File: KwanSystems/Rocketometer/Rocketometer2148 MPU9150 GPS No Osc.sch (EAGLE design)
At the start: 65 parts, among them J001 USB_MICROB_JSTGCT, J301 JST 2mm, J401 M07, J501 GP-2106, J701 MICROSD-SOCKET, Q050 PMOS, Q501 SSM6N58NU, Q502 SSM6N58NU, U101 BMP180, U201 5319 3.3V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

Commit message: j
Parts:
- removed C403, C405: 22pF, SparkFun:CAP0402-CAP
- removed Q501, Q502: SSM6N58NU, KwanSystems:SSM6N58NU
- removed R302: 1M, KwanSystems:RP2EXB24V
- removed R501, R502: 10k, KwanSystems:RP404
- removed Y402: 32kiHz, KwanSystems:ABS06
- added S441: B3U-1100P, KwanSystems:B3U-1100P
- added U502: TXB0104RUT, KwanSystems:TXB0104RUT
- J401: device SparkFun-Connectors:M081X08 -> SparkFun-Connectors:M11PTH
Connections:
- net N$4 renamed CHARGE_STAT-
- net N$8 renamed VEXT
- removed net N$3: D301.A, R053D.1
- removed net RTXC1: C403.2, U401.RTXC1, Y402.2
- removed net RTXC2: C405.1, U401.RTXC2, Y402.1
- new net CHARGE_STAT+: D301.A, R053B.1
- new net EXT: J401.11, U401.(AD1.7/CAP0.0/MAT0.0)P0.22
- net 1.8V: now also U502HEAD.OE, U502HEAD.VCC_LO; no longer Q501A.G, Q501B.G, Q502A.G, Q502B.G, R501B.2, R501C.2, R502B.2, R502C.2
- net 1PPS_I: now also U502D.IO_LO; no longer Q502B.S, R502B.1
- net BATLVL: no longer R302A.2, R302B.2
- net BSL: now also J401.8, S441S.1; no longer J401.5
- net CONN_D+: now also R053A.2; no longer R053B.2
- net EN: no longer U501.EN
- net GND: now also R053C.2, S441G.1, S441S.2, U502HEAD.GND; no longer C403.1, C405.2, R053A.1, R302A.1
- net N$6: now also R053A.1; no longer R053B.1
- net N$7: now also R053C.1; no longer R053A.2
- net ONOFF: now also U502C.IO_HI; no longer Q502A.D, R502A.1
- net ONOFF_I: now also U502C.IO_LO; no longer Q502A.S, R502C.1
- net PPS: now also U502D.IO_HI; no longer Q502B.D, R502D.1
- net RX_GPS: now also J401.5, U502B.IO_HI; no longer J401.6, Q501A.D, R501D.1
- net RX_I: now also U502B.IO_LO; no longer Q501A.S, R501B.1
- net SCL0: now also J401.9
- net SDA0: now also J401.10
- net TX_GPS: now also J401.6, U502A.IO_HI; no longer J401.7, Q501B.D, R501A.1
- net TX_O: now also U502A.IO_LO; no longer Q501B.S, R501C.1
- net USBD+: now also C023A.1; no longer C023B.1
- net USBD-: now also C023B.1; no longer C023A.1
- net VBUS: now also R053B.2; no longer R053D.2
- net VCC: now also J401.7, U401.RTXC1, U501.EN, U502HEAD.VCC_HI; no longer J401.8, R501A.2, R501D.2, R502A.2, R502D.2
- net VLIPO: no longer R302B.1
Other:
- note removed: "OR Y401/C461/C462"
- note removed: "Place either Y403/C404"
- note removed: "but not both groups"
- moved on the sheet: C023A, C023B, C449, C504, C505, R053A, R053B, R053D

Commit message: Finally found a complete solution
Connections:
- removed net N$6: D050.A, Q050.D, R053A.1
- removed net N$7: D050.C, R053C.1
- new net USBLIGHT+: D050.A, R053B.2
- new net USBON+: Q050.D, R053A.2, R053B.1
- net CHARGE_STAT+: now also R053C.2; no longer R053B.1
- net CONN_D+: now also R023A.2, R053A.1; no longer R023B.1, R053A.2
- net CONN_D-: now also R023B.2; no longer R023A.1
- net GND: now also D050.C; no longer R053C.2
- net USBD+: now also R023A.1; no longer R023B.2
- net USBD-: now also R023B.1; no longer R023A.2
- net USB_SOFTCONNECT: now also R015A.1; no longer R015A.2
- net VBUS: now also R053C.1; no longer R053B.2
- net VCC: now also R015A.2; no longer R015A.1
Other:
- moved on the sheet: R023A, R023B, R053A, R053B, R053C
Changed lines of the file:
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@@
 <attribute name="DIGIKEY" x="40.64" y="22.86" size="1.778" layer="96" display="off"/>
 </instance>
-<instance part="D050" gate="G$1" x="22.86" y="66.04" smashed="yes" rot="MR0">
-<attribute name="NAME" x="19.304" y="61.468" size="1.778" layer="95" rot="MR90"/>
-<attribute name="VALUE" x="27.305" y="61.468" size="1.778" layer="96" rot="MR90"/>
-<attribute name="DIGIKEY" x="22.86" y="66.04" size="1.778" layer="96" display="off"/>
+<instance part="D050" gate="G$1" x="22.86" y="48.26" smashed="yes" rot="MR0">
+<attribute name="VALUE" x="27.305" y="43.688" size="1.778" layer="96" rot="MR90"/>
+<attribute name="DIGIKEY" x="22.86" y="48.26" size="1.778" layer="96" display="off"/>
 </instance>
 <instance part="Q050" gate="G$1" x="22.86" y="76.2" rot="R180">
@@
 <attribute name="DIGIKEY" x="205.74" y="40.64" size="1.778" layer="96" display="off"/>
 </instance>
-<instance part="R023" gate="A" x="55.88" y="38.1"/>
-<instance part="R023" gate="B" x="48.26" y="35.56"/>
-<instance part="R053" gate="A" x="17.78" y="55.88" rot="R270">
-<attribute name="DIGIKEY" x="17.78" y="55.88" size="1.778" layer="96" display="off"/>
-</instance>
-<instance part="R053" gate="C" x="22.86" y="48.26" rot="R270"/>
+<instance part="R023" gate="B" x="55.88" y="38.1"/>
+<instance part="R023" gate="A" x="48.26" y="35.56"/>
+<instance part="R053" gate="A" x="17.78" y="58.42" rot="R270">
+<attribute name="DIGIKEY" x="17.78" y="58.42" size="1.778" layer="96" display="off"/>
+</instance>
+<instance part="R053" gate="B" x="22.86" y="58.42" rot="R90"/>
 <instance part="C023" gate="A" x="71.12" y="20.32">
 <attribute name="DIGIKEY" x="71.12" y="20.32" size="1.778" layer="96" display="off"/>
@@
 </instance>
 <instance part="R015" gate="B" x="63.5" y="40.64" rot="R180"/>
-<instance part="R053" gate="B" x="114.3" y="27.94" rot="R90"/>
+<instance part="R053" gate="C" x="114.3" y="27.94" rot="R90"/>
 <instance part="D401" gate="B" x="218.44" y="-58.42" rot="R270">
 <attribute name="DIGIKEY" x="218.44" y="-58.42" size="1.778" layer="96" display="off"/>
@@
 <wire x1="276.86" y1="86.36" x2="276.86" y2="88.9" width="0.1524" layer="91"/>
 <wire x1="276.86" y1="45.72" x2="276.86" y2="86.36" width="0.1524" layer="91"/>
-<wire x1="22.86" y1="86.36" x2="38.1" y2="86.36" width="0.1524" layer="91"/>
-<wire x1="38.1" y1="86.36" x2="276.86" y2="86.36" width="0.1524" layer="91"/>
+<wire x1="22.86" y1="86.36" x2="38.1" y2="76.2" width="0.1524" layer="91"/>
+<wire x1="38.1" y1="76.2" x2="276.86" y2="86.36" width="0.1524" layer="91"/>
 <wire x1="22.86" y1="86.36" x2="22.86" y2="81.28" width="0.1524" layer="91"/>
 <wire x1="261.62" y1="45.72" x2="276.86" y2="45.72" width="0.1524" layer="91"/>
@@
 <pinref part="U201" gate="G$1" pin="VOUT"/>
 <pinref part="C205" gate="G$1" pin="1"/>
-<pinref part="R015" gate="A" pin="1"/>
-<junction x="38.1" y="86.36"/>
+<pinref part="R015" gate="A" pin="2"/>
+<junction x="38.1" y="76.2"/>
 </segment>
 <segment>
@@
 <wire x1="12.7" y1="12.7" x2="12.7" y2="15.24" width="0.1524" layer="91"/>
 <wire x1="40.64" y1="15.24" x2="40.64" y2="17.78" width="0.1524" layer="91"/>
-<wire x1="22.86" y1="43.18" x2="22.86" y2="15.24" width="0.1524" layer="91"/>
-<wire x1="22.86" y1="15.24" x2="12.7" y2="15.24" width="0.1524" layer="91"/>
 <wire x1="71.12" y1="17.78" x2="71.12" y2="15.24" width="0.1524" layer="91"/>
 <wire x1="71.12" y1="15.24" x2="40.64" y2="15.24" width="0.1524" layer="91"/>
 <wire x1="40.64" y1="15.24" x2="22.86" y2="15.24" width="0.1524" layer="91"/>
+<wire x1="22.86" y1="15.24" x2="12.7" y2="15.24" width="0.1524" layer="91"/>
 <wire x1="81.28" y1="17.78" x2="81.28" y2="15.24" width="0.1524" layer="91"/>
 <wire x1="81.28" y1="15.24" x2="71.12" y2="15.24" width="0.1524" layer="91"/>
@@
 <junction x="12.7" y="15.24"/>
 <junction x="40.64" y="15.24"/>
-<junction x="22.86" y="15.24"/>
 <junction x="71.12" y="15.24"/>
 <junction x="81.28" y="15.24"/>
@@
 <pinref part="U301" gate="G$1" pin="VSS"/>
 <pinref part="S201" gate="B" pin="P$1"/>
-<pinref part="R053" gate="C" pin="2"/>
 <pinref part="C023" gate="A" pin="2"/>
 <pinref part="C023" gate="B" pin="2"/>
+<pinref part="D050" gate="G$1" pin="C"/>
+<wire x1="22.86" y1="43.18" x2="22.86" y2="15.24" width="0.1524" layer="91"/>
+<junction x="22.86" y="15.24"/>
 </segment>
 <segment>
@@
 <wire x1="33.02" y1="33.02" x2="101.6" y2="33.02" width="0.1524" layer="91"/>
 <wire x1="101.6" y1="30.48" x2="101.6" y2="33.02" width="0.1524" layer="91"/>
-<wire x1="124.46" y1="33.02" x2="114.3" y2="33.02" width="0.1524" layer="91"/>
-<wire x1="114.3" y1="33.02" x2="109.22" y2="33.02" width="0.1524" layer="91"/>
+<wire x1="124.46" y1="33.02" x2="114.3" y2="22.86" width="0.1524" layer="91"/>
+<wire x1="114.3" y1="22.86" x2="109.22" y2="33.02" width="0.1524" layer="91"/>
 <junction x="40.64" y="40.64"/>
 <junction x="33.02" y="40.64"/>
 <junction x="101.6" y="33.02"/>
 <junction x="109.22" y="33.02"/>
-<junction x="114.3" y="33.02"/>
+<junction x="114.3" y="22.86"/>
 <label x="91.44" y="33.02" size="1.778" layer="95"/>
 <pinref part="D302" gate="G$1" pin="A1"/>
@@
 <pinref part="U301" gate="G$1" pin="VIN"/>
 <pinref part="R015" gate="B" pin="2"/>
-<pinref part="R053" gate="B" pin="2"/>
+<pinref part="R053" gate="C" pin="1"/>
 </segment>
 </net>
@@
 </segment>
 <segment>
-<wire x1="60.96" y1="38.1" x2="81.28" y2="38.1" width="0.1524" layer="91"/>
+<wire x1="50.8" y1="38.1" x2="81.28" y2="38.1" width="0.1524" layer="91"/>
 <wire x1="81.28" y1="38.1" x2="81.28" y2="63.5" width="0.1524" layer="91"/>
 <wire x1="81.28" y1="38.1" x2="81.28" y2="25.4" width="0.1524" layer="91"/>
 <junction x="81.28" y="38.1"/>
 <label x="81.28" y="63.5" size="1.778" layer="95" rot="MR270"/>
-<pinref part="R023" gate="A" pin="2"/>
+<pinref part="R023" gate="B" pin="1"/>
 <pinref part="C023" gate="B" pin="1"/>
 </segment>
@@
 </segment>
 <segment>
-<wire x1="53.34" y1="35.56" x2="71.12" y2="35.56" width="0.1524" layer="91"/>
+<wire x1="43.18" y1="35.56" x2="71.12" y2="35.56" width="0.1524" layer="91"/>
 <wire x1="71.12" y1="35.56" x2="71.12" y2="43.18" width="0.1524" layer="91"/>
 <wire x1="71.12" y1="43.18" x2="78.74" y2="43.18" width="0.1524" layer="91"/>
@@
 <junction x="71.12" y="35.56"/>
 <label x="78.74" y="63.5" size="1.778" layer="95" rot="MR270"/>
-<pinref part="R023" gate="B" pin="2"/>
+<pinref part="R023" gate="A" pin="1"/>
 <pinref part="C023" gate="A" pin="1"/>
 </segment>
@@
 </segment>
 <segment>
-<wire x1="30.48" y1="76.2" x2="38.1" y2="76.2" width="0.1524" layer="91"/>
-<wire x1="38.1" y1="76.2" x2="38.1" y2="45.72" width="0.1524" layer="91"/>
+<wire x1="30.48" y1="76.2" x2="38.1" y2="86.36" width="0.1524" layer="91"/>
+<wire x1="38.1" y1="86.36" x2="38.1" y2="45.72" width="0.1524" layer="91"/>
 <wire x1="38.1" y1="45.72" x2="76.2" y2="45.72" width="0.1524" layer="91"/>
 <wire x1="76.2" y1="45.72" x2="76.2" y2="63.5" width="0.1524" layer="91"/>
 <label x="76.2" y="63.5" size="1.778" layer="95" rot="MR270"/>
 <pinref part="Q050" gate="G$1" pin="G"/>
-<pinref part="R015" gate="A" pin="2"/>
-<junction x="38.1" y="76.2"/>
+<pinref part="R015" gate="A" pin="1"/>
+<junction x="38.1" y="86.36"/>
 </segment>
 </net>
@@
 <net name="CONN_D-" class="0">
 <segment>
-<wire x1="2.54" y1="38.1" x2="50.8" y2="38.1" width="0.1524" layer="91"/>
+<wire x1="2.54" y1="38.1" x2="60.96" y2="38.1" width="0.1524" layer="91"/>
 <pinref part="J001" gate="G$1" pin="D-"/>
-<pinref part="R023" gate="A" pin="1"/>
+<pinref part="R023" gate="B" pin="2"/>
 </segment>
 </net>
@@
 <segment>
 <wire x1="2.54" y1="35.56" x2="17.78" y2="35.56" width="0.1524" layer="91"/>
-<wire x1="17.78" y1="35.56" x2="43.18" y2="35.56" width="0.1524" layer="91"/>
-<wire x1="17.78" y1="50.8" x2="17.78" y2="35.56" width="0.1524" layer="91"/>
+<wire x1="17.78" y1="35.56" x2="53.34" y2="35.56" width="0.1524" layer="91"/>
+<wire x1="17.78" y1="63.5" x2="17.78" y2="35.56" width="0.1524" layer="91"/>
 <junction x="17.78" y="35.56"/>
 <pinref part="J001" gate="G$1" pin="D+"/>
-<pinref part="R023" gate="B" pin="1"/>
-<pinref part="R053" gate="A" pin="2"/>
-</segment>
-</net>
-<net name="N$7" class="0">
-<segment>
-<wire x1="22.86" y1="60.96" x2="22.86" y2="53.34" width="0.1524" layer="91"/>
-<pinref part="D050" gate="G$1" pin="C"/>
-<pinref part="R053" gate="C" pin="1"/>
+<pinref part="R023" gate="A" pin="2"/>
+<pinref part="R053" gate="A" pin="1"/>
 </segment>
 </net>
 <net name="CHARGE_STAT+" class="0">
 <segment>
-<wire x1="114.3" y1="22.86" x2="114.3" y2="20.32" width="0.1524" layer="91"/>
+<wire x1="114.3" y1="33.02" x2="114.3" y2="20.32" width="0.1524" layer="91"/>
 <wire x1="114.3" y1="20.32" x2="121.92" y2="20.32" width="0.1524" layer="91"/>
 <pinref part="D301" gate="G$1" pin="A"/>
-<pinref part="R053" gate="B" pin="1"/>
+<pinref part="R053" gate="C" pin="2"/>
 </segment>
 </net>
@@
 </segment>
 </net>
-<net name="N$6" class="0">
+<net name="USBON+" class="0">
 <segment>
 <wire x1="22.86" y1="71.12" x2="22.86" y2="68.58" width="0.1524" layer="91"/>
-<wire x1="22.86" y1="68.58" x2="17.78" y2="68.58" width="0.1524" layer="91"/>
-<wire x1="17.78" y1="68.58" x2="17.78" y2="60.96" width="0.1524" layer="91"/>
-<junction x="22.86" y="68.58"/>
 <pinref part="Q050" gate="G$1" pin="D"/>
-<pinref part="D050" gate="G$1" pin="A"/>
-<pinref part="R053" gate="A" pin="1"/>
+<pinref part="R053" gate="A" pin="2"/>
+<wire x1="17.78" y1="53.34" x2="17.78" y2="68.58" width="0.1524" layer="91"/>
+<wire x1="17.78" y1="68.58" x2="22.86" y2="68.58" width="0.1524" layer="91"/>
+<pinref part="R053" gate="B" pin="1"/>
+<wire x1="22.86" y1="68.58" x2="22.86" y2="53.34" width="0.1524" layer="91"/>
 </segment>
 </net>
@@
 </segment>
 </net>
+<net name="USBLIGHT+" class="0">
+<segment>
+<pinref part="D050" gate="G$1" pin="A"/>
+<pinref part="R053" gate="B" pin="2"/>
+<wire x1="22.86" y1="63.5" x2="22.86" y2="50.8" width="0.1524" layer="91"/>
+</segment>
+</net>

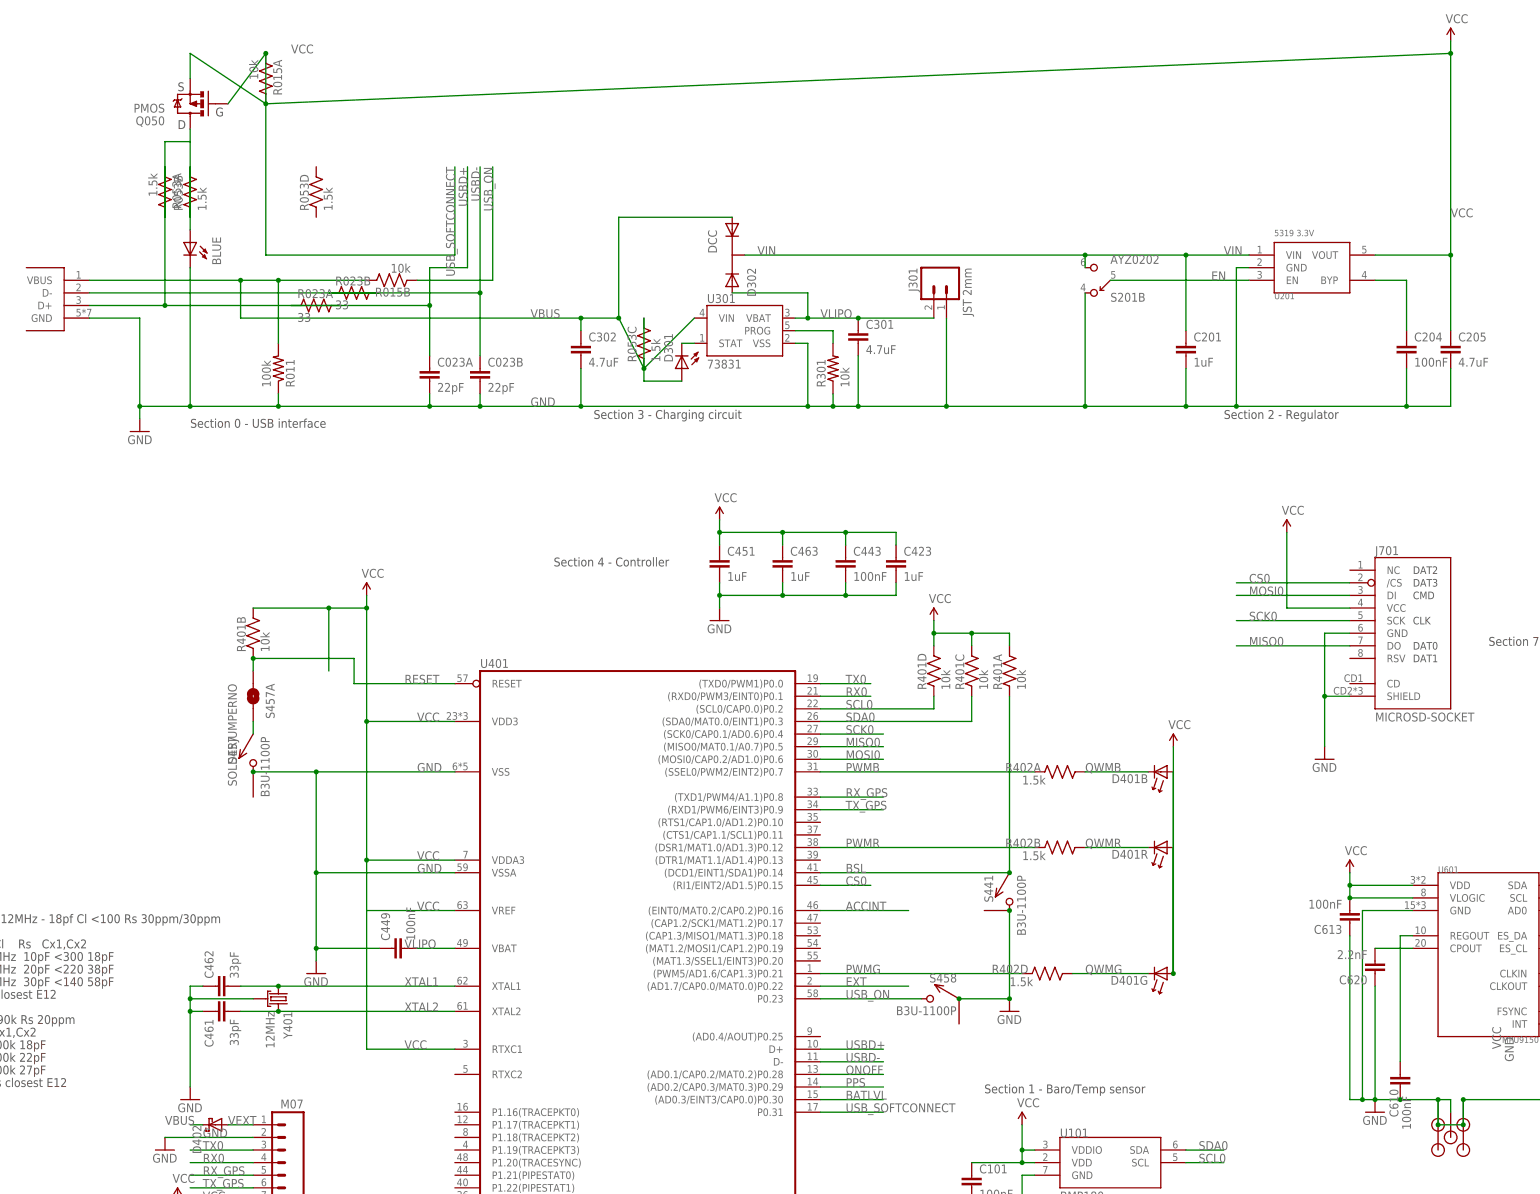
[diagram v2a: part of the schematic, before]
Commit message: Added new feature to NavCalc
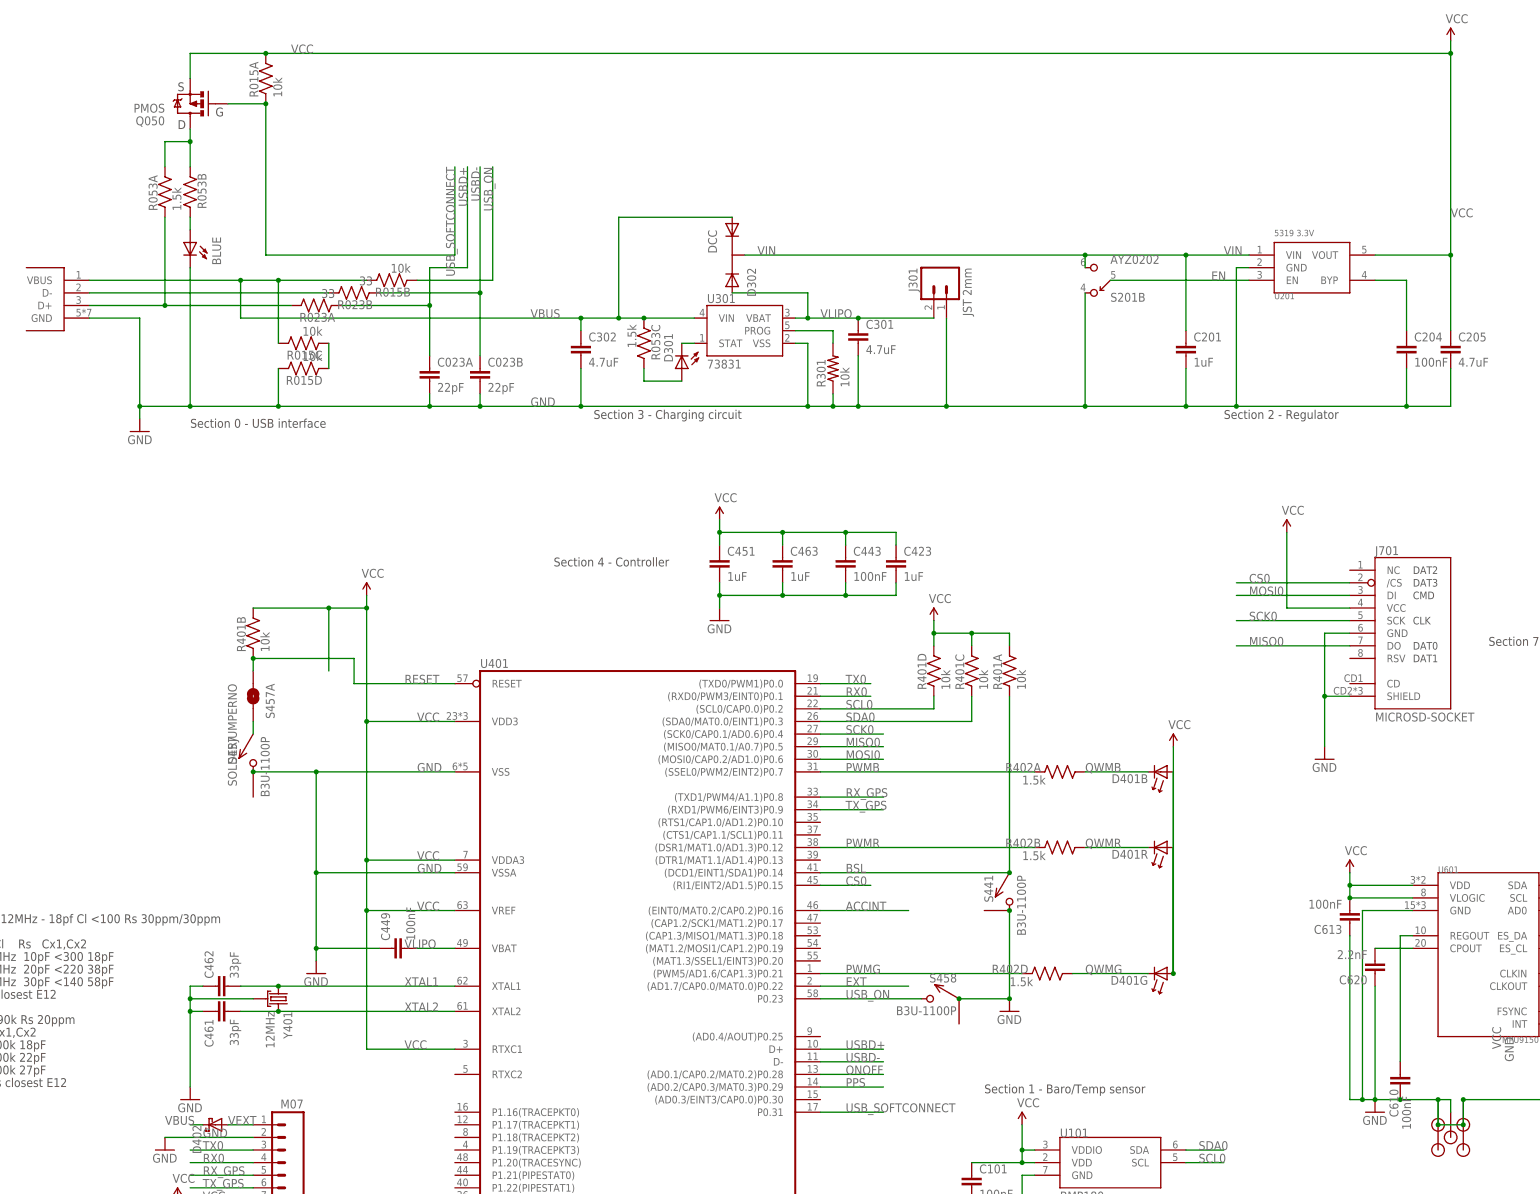
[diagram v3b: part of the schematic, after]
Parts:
- removed R011: 100k, SparkFun:RESISTOR0402-RES
- R015: device KwanSystems:RP2EXB24V -> KwanSystems:RP404
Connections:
- removed net BATLVL: U401.(AD0.3/EINT3/CAP0.0)P0.30
- new net N$3: R015C.1, R015D.1
- net GND: now also R015D.2; no longer R011.1
- net VBUS: now also R015C.2; no longer R011.2
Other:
- moved on the sheet: R015A, R023A, R023B, R053A, R053B, R053C
